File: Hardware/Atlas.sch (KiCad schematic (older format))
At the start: 47 parts, among them J1 DC, U1 MS5611, U2 HTU21D, U3 uSD Card, U4 RFD900, U5 MPU9150, U6 XBEE, U7 VENUS838FLPX-L, U8 AOZ1031

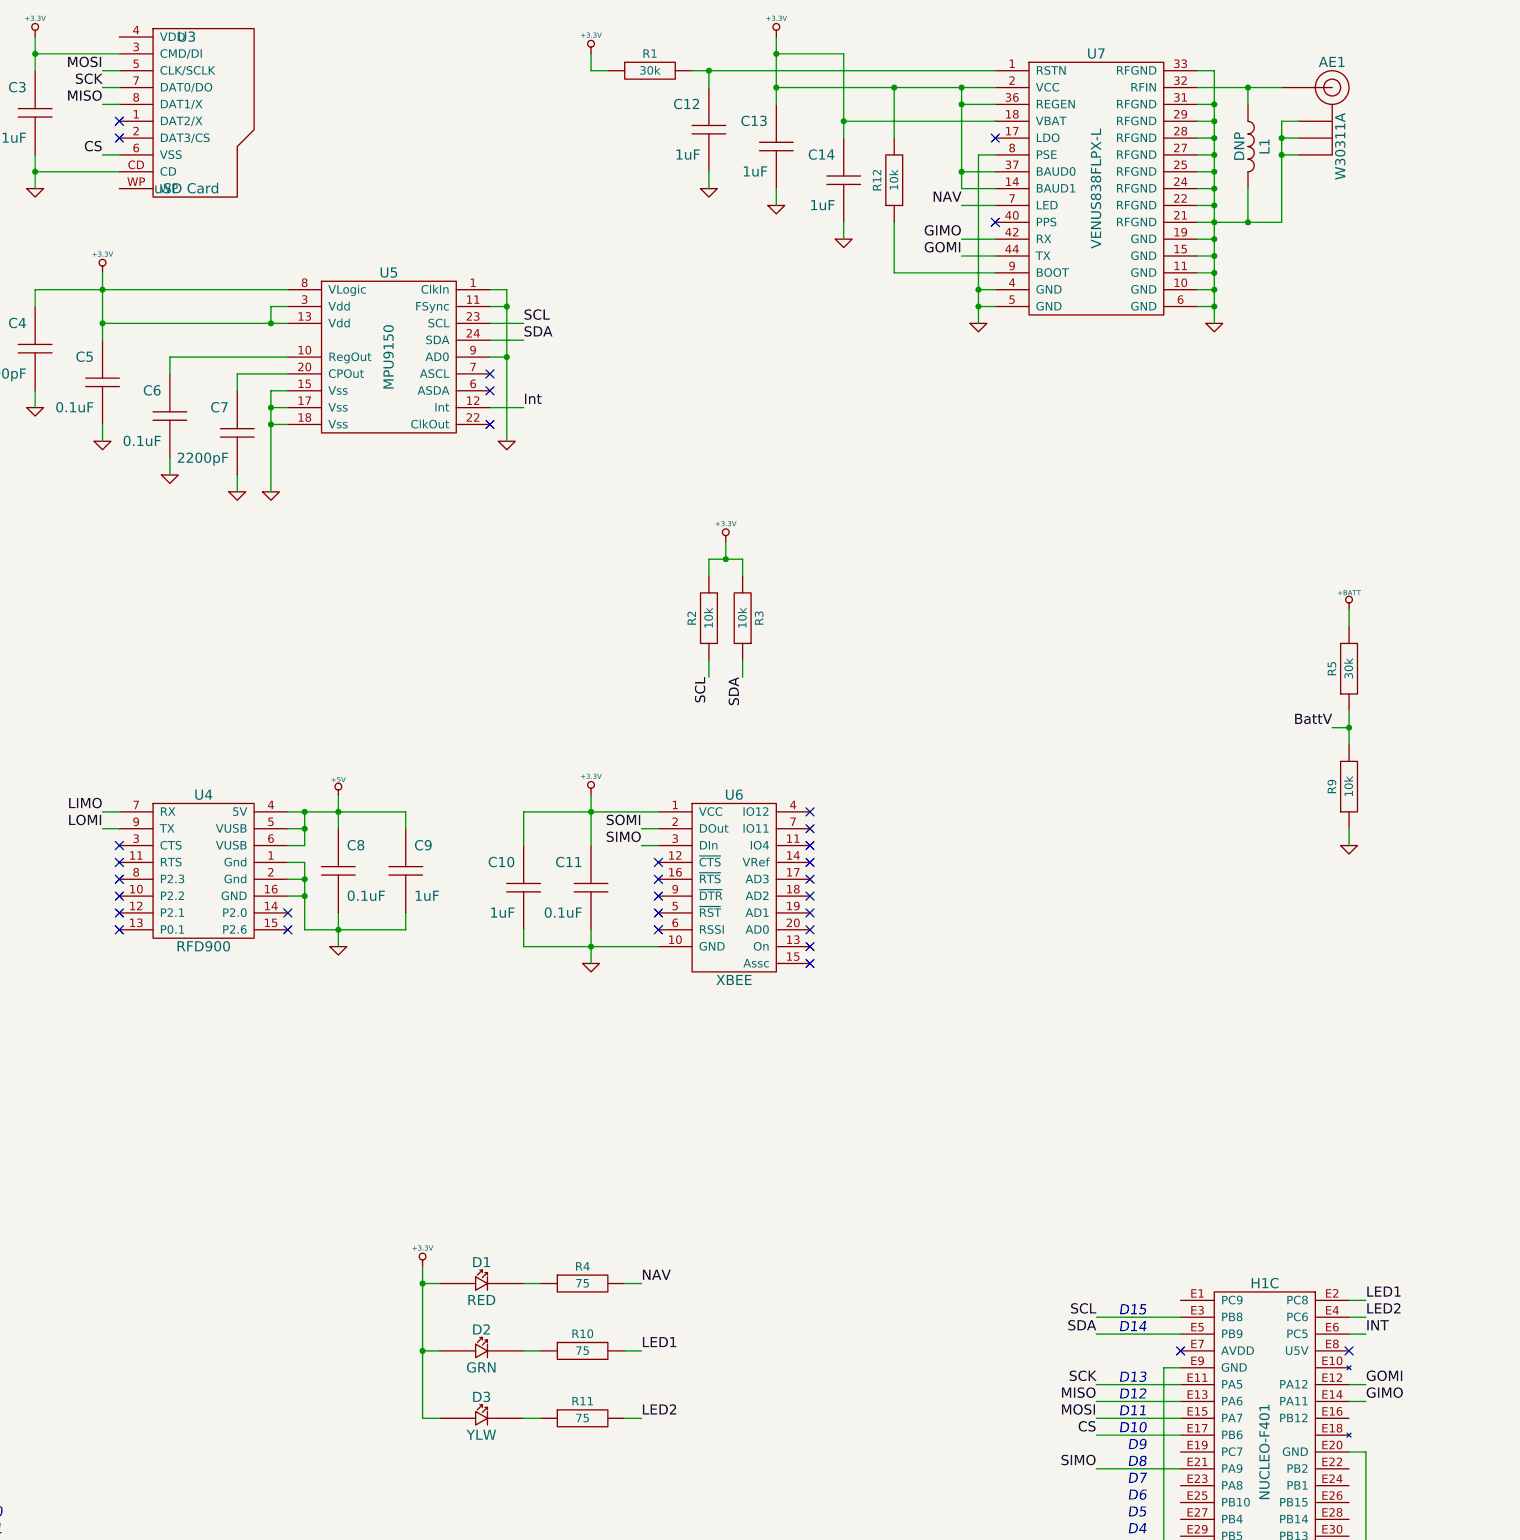
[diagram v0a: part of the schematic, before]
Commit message: Connect GPS PPS output
Closes #5
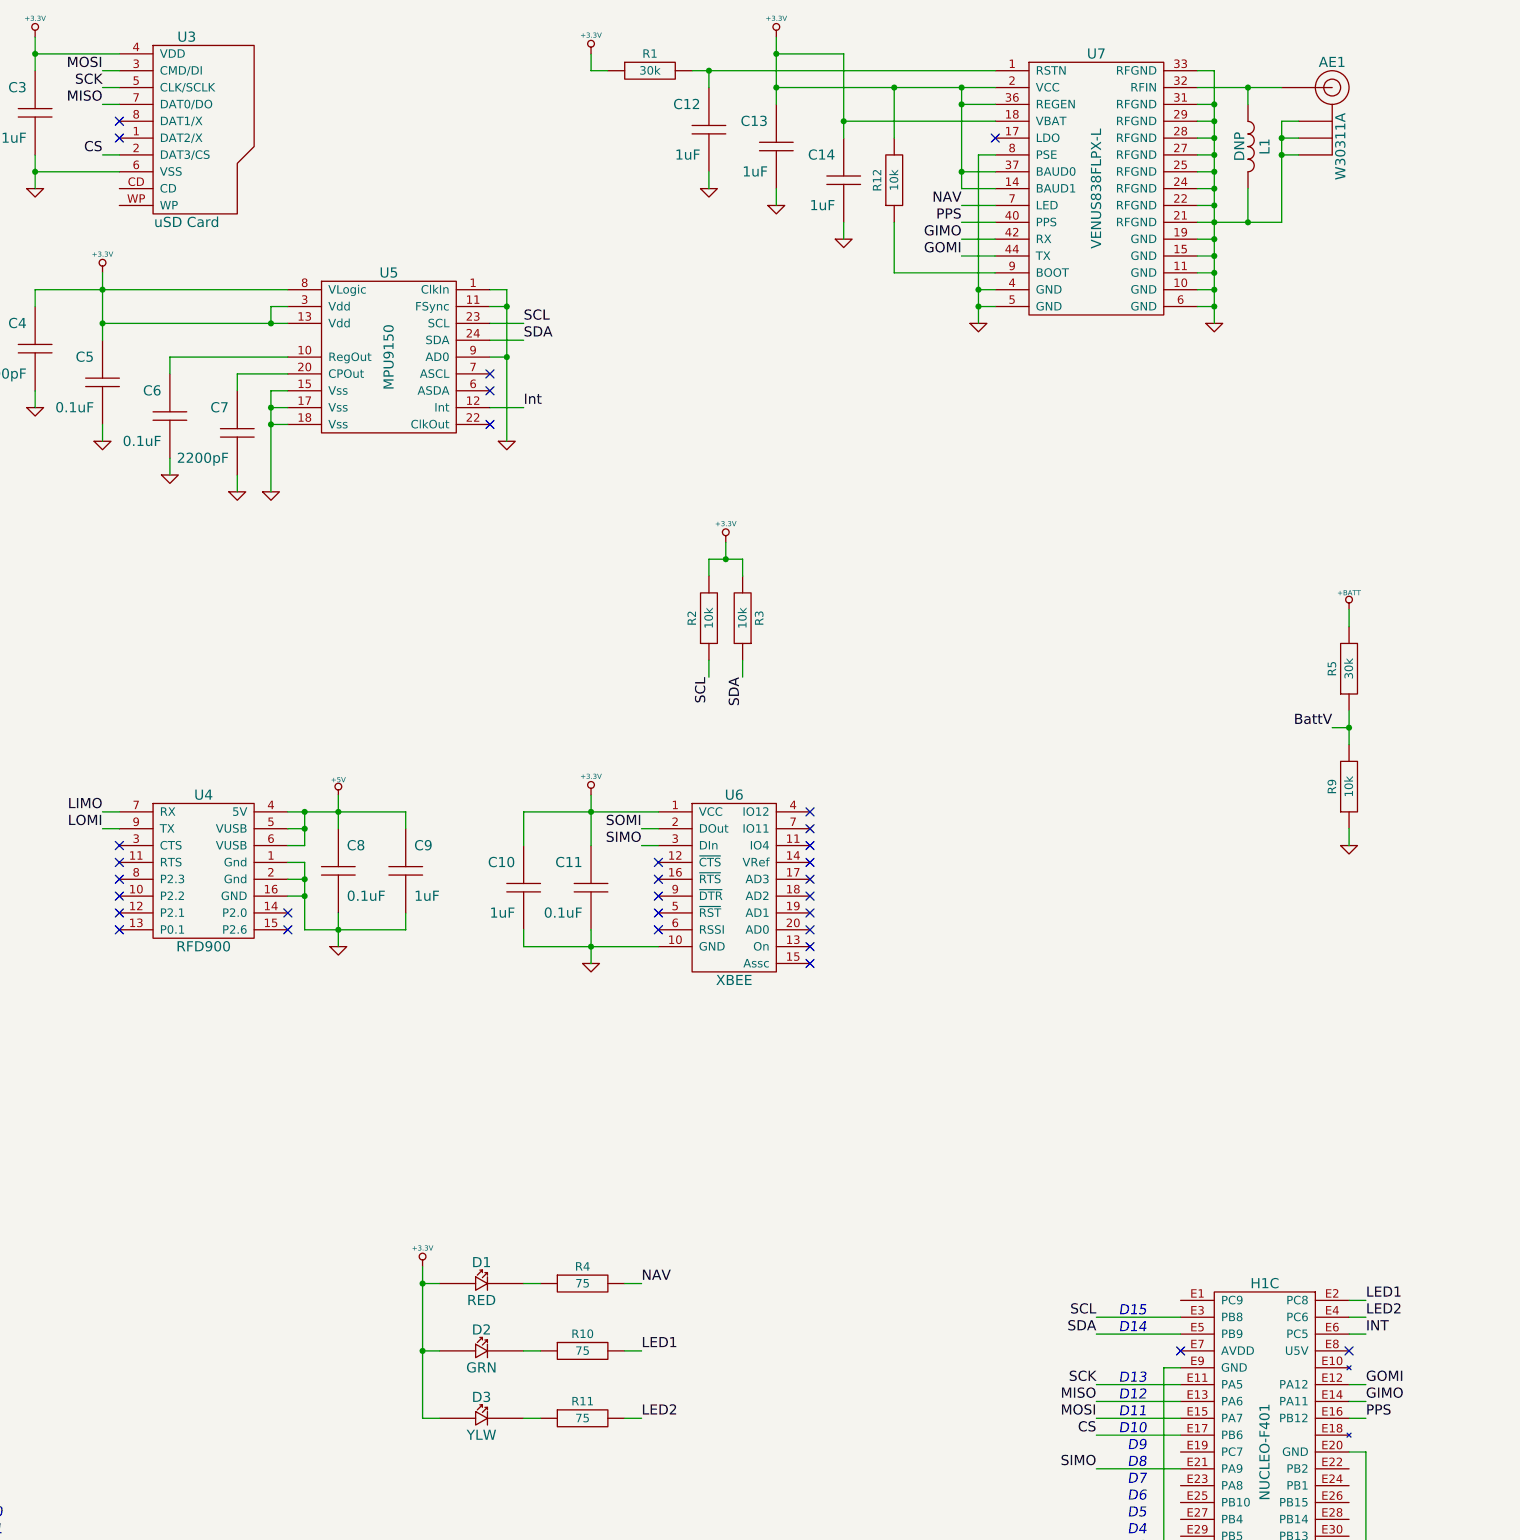
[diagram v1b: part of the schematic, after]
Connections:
- net +3.3V: now also U3.4 (VDD); no longer U3.3 (CMD/DI)
- net CS: now also U3.2 (DAT3/CS); no longer U3.6 (VSS)
- net GND: now also U3.6 (VSS); no longer U3.CD
- net MISO: now also U3.7 (DAT0/DO); no longer U3.8 (DAT1/X)
- net MOSI: now also U3.3 (CMD/DI); no longer U3.5 (CLK/SCLK)
- net SCK: now also U3.5 (CLK/SCLK); no longer U3.7 (DAT0/DO)
- net PPS: now reaches H1.E16 (PB12)
- net PPS: now also U7.40 (PPS)
- no-connect marks 44 -> 43
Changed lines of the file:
@@
 Sheet 1 1
 Title "Atlas (Nucleo Shield)"
-Date "3 jun 2014"
+Date "18 oct 2014"
 Rev "1"
 Comp "Aerodyne Labs"
@@
 $EndComp
 $Comp
-L SDCARD-FULL-MICRO U3
-U 1 1 537D2B6A
-P 4000 1350
-F 0 "U3" H 4000 1800 60  0000 C CNN
-F 1 "uSD Card" H 4000 900 60  0000 C CNN
-F 2 "~" H 4000 1350 60  0000 C CNN
-F 3 "~" H 4000 1350 60  0000 C CNN
-F 4 "Amphenol" H 4000 1350 60  0001 C CNN "MFR Name"
-F 5 "101-00303-68" H 4000 1350 60  0001 C CNN "MFR Part No"
-F 6 "101-00303-68-1-ND" H 4000 1350 60  0001 C CNN "Distributor Part No"
-	1    4000 1350
-	-1   0    0    -1
-$EndComp
-$Comp
 L RFD900 U4
 U 1 1 537D3811
@@
 	1    0    0    -1
 $EndComp
-NoConn ~ 8800 2000
 $Comp
 L GND #PWR020
@@
 	1    0    0    -1
 $EndComp
+Text Label 8600 2000 2    60   ~ 0
+PPS
+Wire Wire Line
+	8600 2000 8800 2000
+Text Label 11000 9100 0    60   ~ 0
+PPS
+$Comp
+L SDCARD-FULL-MICRO U3
+U 1 1 5442EFB9
+P 4000 1450
+F 0 "U3" H 4000 2000 60  0000 C CNN
+F 1 "uSD Card" H 4000 900 60  0000 C CNN
+F 2 "~" H 4000 1550 60  0000 C CNN
+F 3 "~" H 4000 1550 60  0000 C CNN
+F 4 "Amphenol" H 4000 1450 60  0001 C CNN "MFR Name"
+F 5 "101-00303-68" H 4000 1450 60  0001 C CNN "MFR Part No"
+F 6 "101-00303-68-1-ND" H 4000 1450 60  0001 C CNN "Distributor Part No"
+	1    4000 1450
+	-1   0    0    -1
+$EndComp
+Wire Wire Line
+	11000 9100 10900 9100
 $EndSCHEMATC

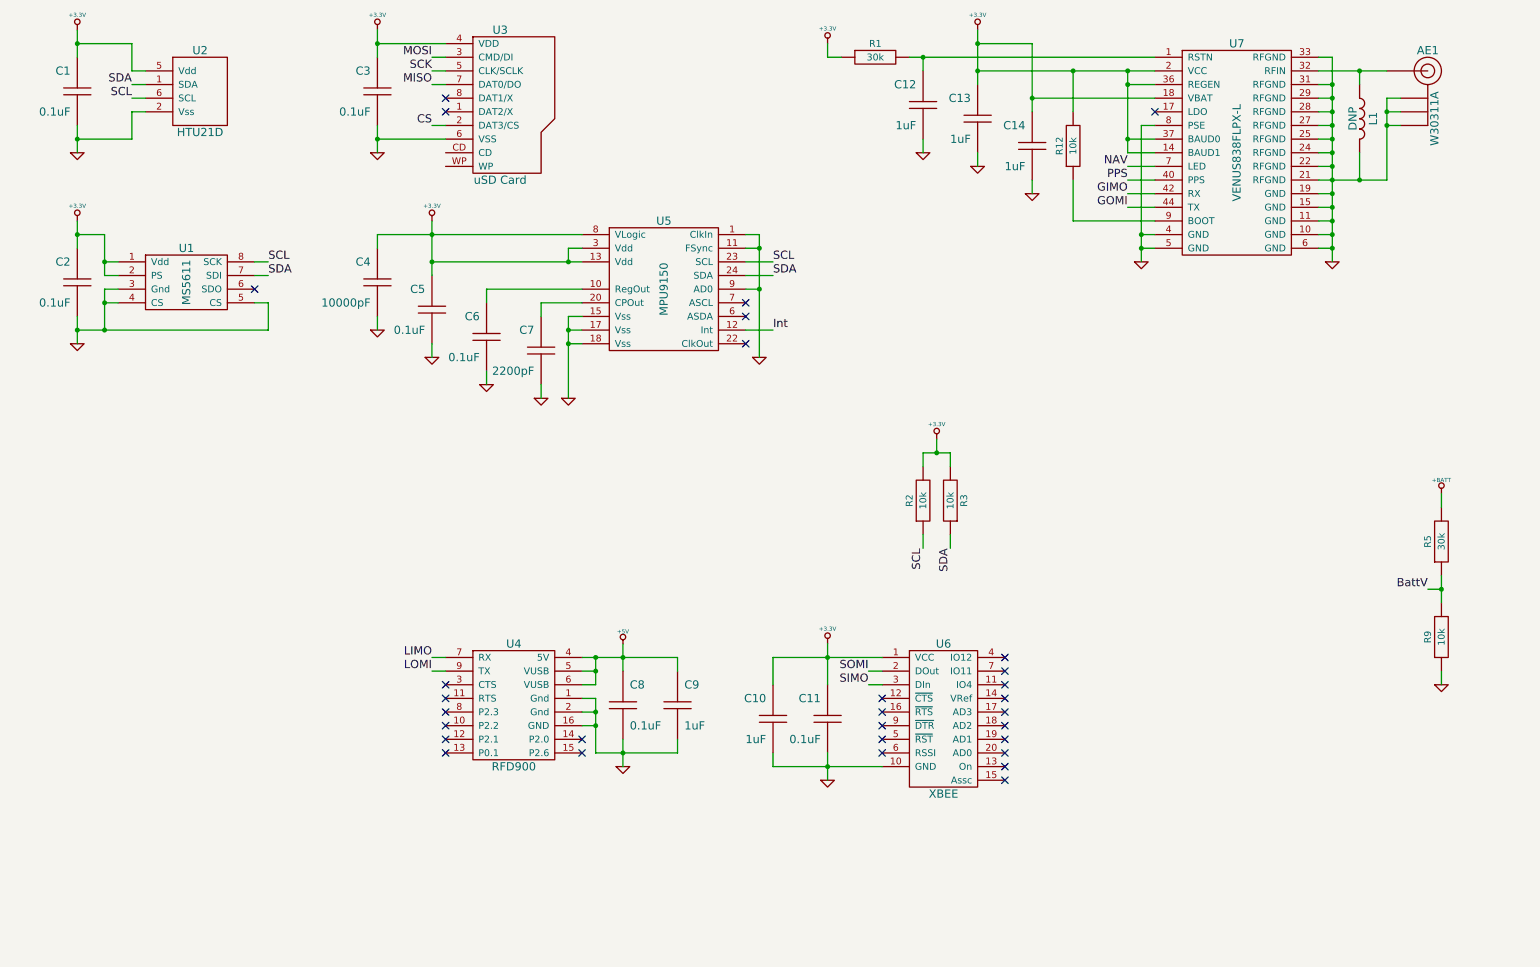
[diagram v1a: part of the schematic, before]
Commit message: Switch GPS to SMA antennas port
Add pull up inductor to support active antenna. Closes #7
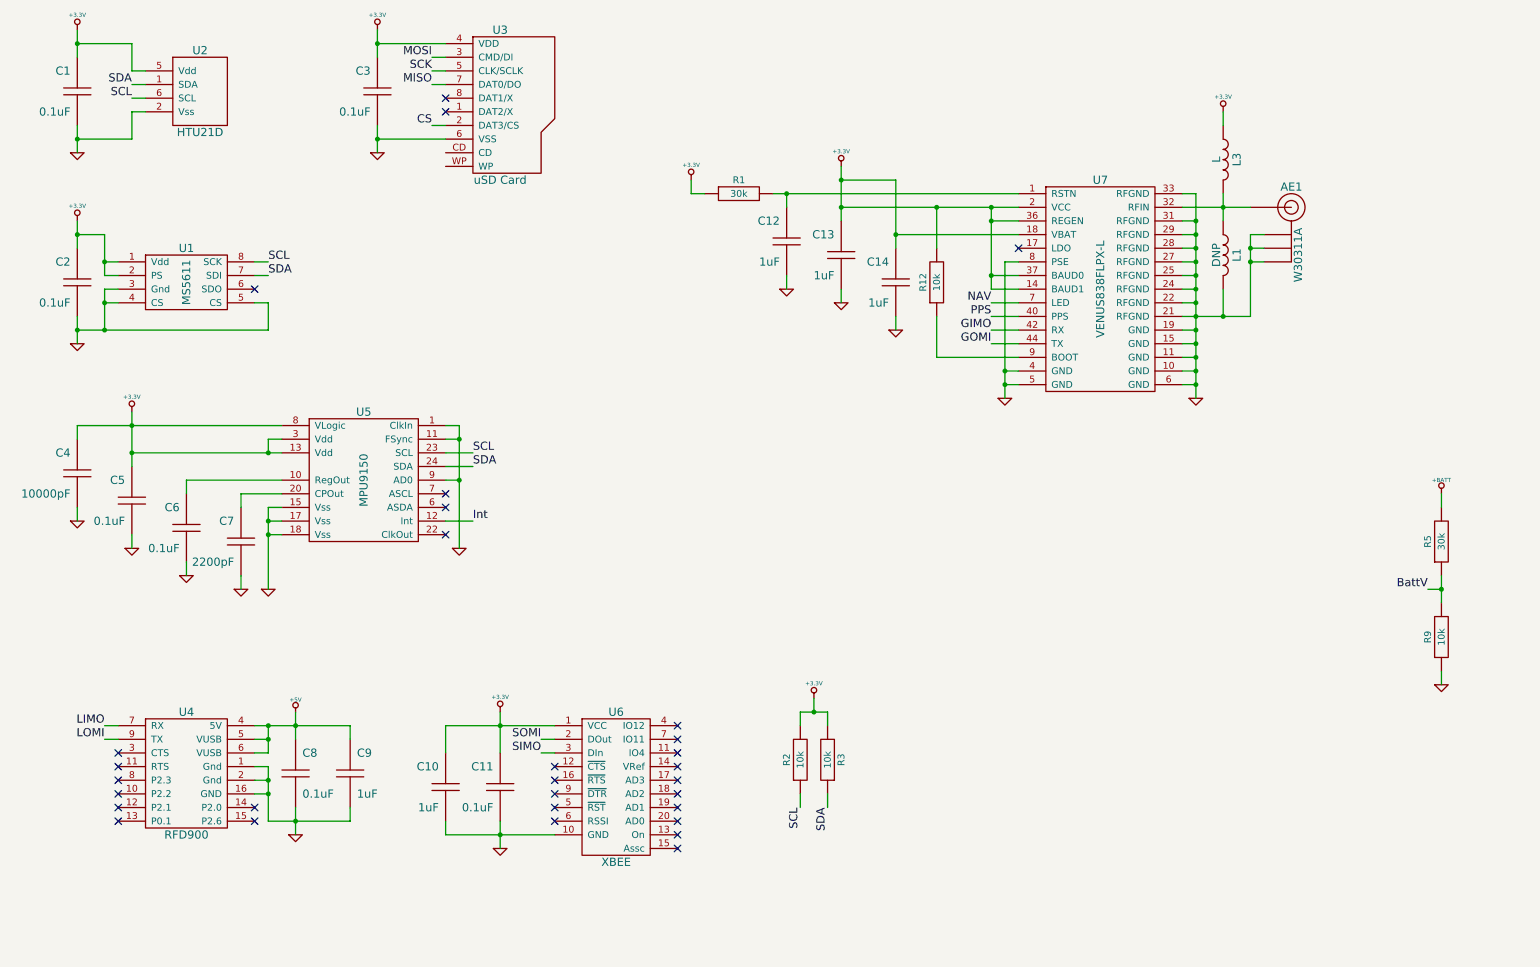
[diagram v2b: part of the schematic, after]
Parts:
- added L3: L, ~, symbol L
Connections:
- net +3.3V: now also L3.2
- net at AE1.P, L1.2, U7.32 (RFIN): now also L3.1
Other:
- moved on the sheet: AE1, C10, C11, C12, C13, C14, C4, C5, C6, C7, C8, C9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
